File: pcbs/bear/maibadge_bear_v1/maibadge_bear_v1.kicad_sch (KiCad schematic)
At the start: 13 parts, among them J1 Conn_01x04_Socket, SW1 SW_Push, SW2 SW_Push, SW3 SW_Push, SW4 SW_Push, U1 AMS1117-3.3, U2 ESP32-S3-WROOM-1

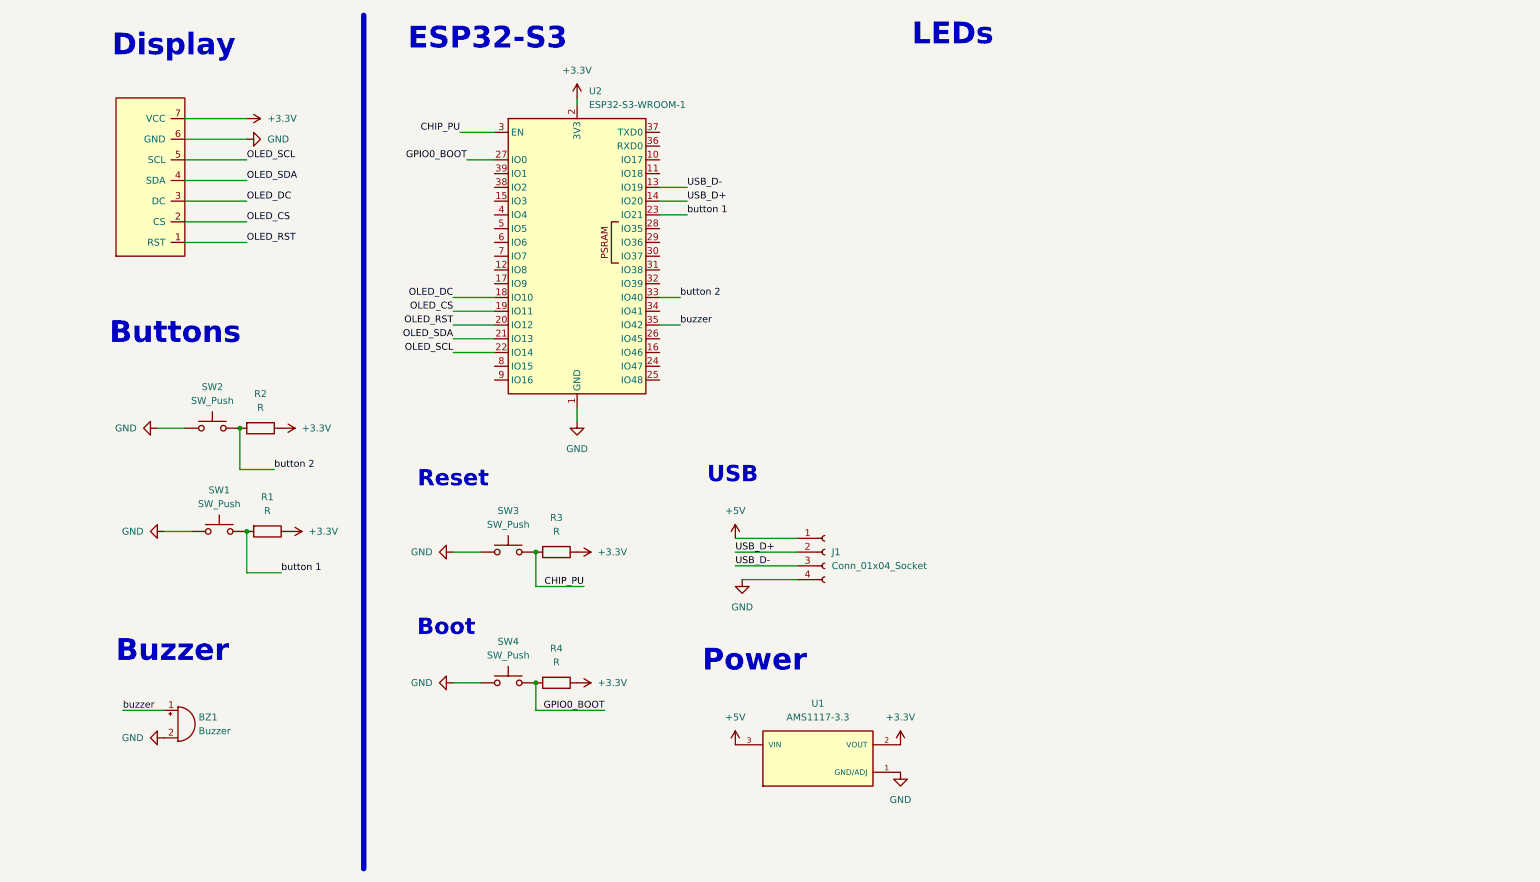
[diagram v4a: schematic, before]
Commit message: added leds and mpr121 for pcb
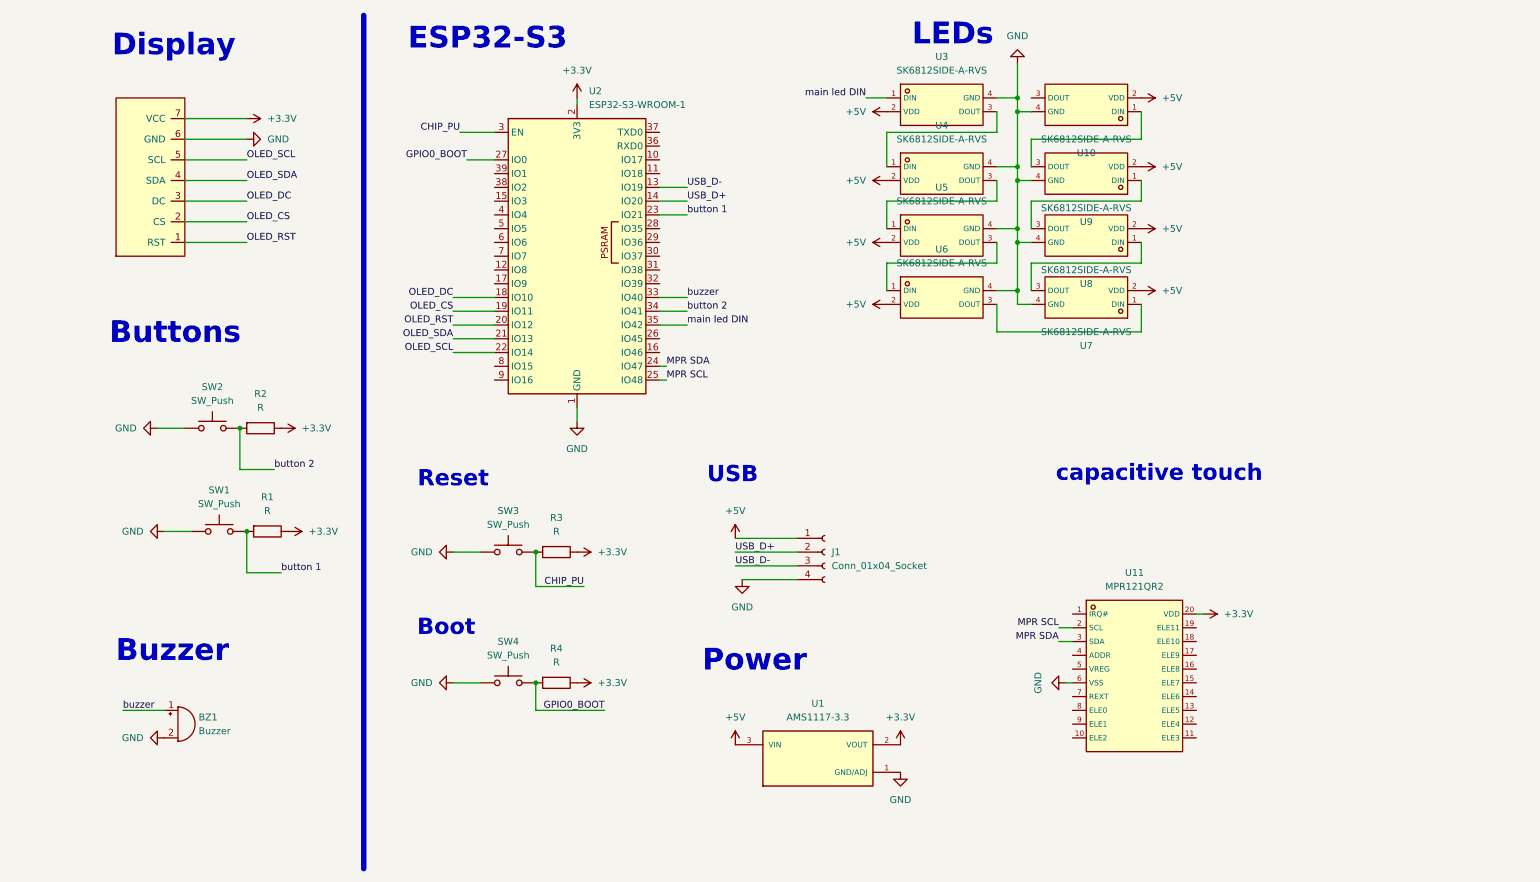
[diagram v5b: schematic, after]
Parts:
- added U10, U3, U4, U5, U6, U7, U8, U9: SK6812SIDE-A-RVS, aeasyeda-footprint:LED-SMD_4P-L4.0-W1.6-L, symbol ask6812:SK6812SIDE-A-RVS
- added U11: MPR121QR2, aeasyeda-footprint:QFN-20_L3.0-W3.0-P0.40-BL, symbol amaibear:MPR121QR2
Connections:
- net +3.3V: now also U11.20 (VDD)
- net +5V: now also U10.2 (VDD), U3.2 (VDD), U4.2 (VDD), U5.2 (VDD), U6.2 (VDD), U7.2 (VDD), U8.2 (VDD), U9.2 (VDD)
- net GND: now also U10.4 (GND), U11.6 (VSS), U3.4 (GND), U4.4 (GND), U5.4 (GND), U6.4 (GND), U7.4 (GND), U8.4 (GND), U9.4 (GND)
- net button 2: now also U2.34 (IO41); no longer U2.33 (IO40)
- net buzzer: now also U2.33 (IO40); no longer U2.35 (IO42)
- net MPR SDA: now reaches U2.24 (IO47)
- net MPR SDA: now also U11.3 (SDA)
- net MPR SCL: now reaches U2.25 (IO48)
- net MPR SCL: now also U11.2 (SCL)
- new net: U3.3 (DOUT), U4.1 (DIN)
- new net: U7.3 (DOUT), U8.1 (DIN)
- new net: U8.3 (DOUT), U9.1 (DIN)
- new net: U5.3 (DOUT), U6.1 (DIN)
- new net: U6.3 (DOUT), U7.1 (DIN)
- new net: U4.3 (DOUT), U5.1 (DIN)
- new net: U10.1 (DIN), U9.3 (DOUT)
- new net main led DIN: U2.35 (IO42), U3.1 (DIN)
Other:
- note added: "capacitive touch"

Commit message: prototype 2 done
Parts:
- removed BZ1: Buzzer, Buzzer_Beeper:MagneticBuzzer_Kobitone_254-EMB73-RO, symbol Device:Buzzer
- removed U11: MPR121QR2, aeasyeda-footprint:QFN-20_L3.0-W3.0-P0.40-BL, symbol amaibear:MPR121QR2
- added JP2: SolderJumper_3_Bridged12, Jumper:SolderJumper-3_P1.3mm_Bridged2Bar12_Pad1.0x1.5mm_NumberLabels, symbol Jumper:SolderJumper_3_Bridged12
- added U12: MS-23C01-G020, aeasyeda-footprint:SW-SMD_G-SWITCH_MS-23C01-G020, symbol amaibear:MS-23C01-G020
- added U13: FUET-7525-3_6V, aeasyeda-footprint:BUZ-SMD_4P-L7.5-W7.5-BR, symbol amaibear:FUET-7525-3_6V
- U1: footprint local_footprints:SOT229P700X180-4N -> aeasyeda-footprint:SOT-89-3_L4.5-W2.5-P1.50-LS4.2-BR
- renumbered U9 to U10, U10 to U3, U3 to U4, U4 to U5, U5 to U6, U6 to U7, U7 to U8, U8 to U9
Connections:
- net MPR SDA is gone; now on net GPIO0_BOOT: U2.24 (IO47)
- net +3.3V: now also JP2.1 (A), U12.2; no longer GC9A01.7 (VCC)
- net +5V: now also JP2.3 (B); no longer U10.2 (VDD), U3.2 (VDD), U4.2 (VDD), U5.2 (VDD), U6.2 (VDD), U7.2 (VDD), U8.2 (VDD), U9.2 (VDD)
- net GND: now also U13.1
- net GPIO0_BOOT: no longer U2.27 (IO0)
- net USB_D+: now also J1.3 (Pin_3), U2.13 (IO19); no longer J1.2 (Pin_2), U2.14 (IO20)
- net USB_D-: now also J1.2 (Pin_2), U2.14 (IO20); no longer J1.3 (Pin_3), U2.13 (IO19)
- net button 2: now also U2.28 (IO35); no longer U2.34 (IO41)
- net buzzer: now also U2.27 (IO0), U13.2; no longer U2.33 (IO40)
- net main led DIN: now also U3.1 (DIN); no longer U4.1 (DIN)
- net touch_sensor_8: now reaches U2.12 (IO8)
- net touch_sensor_3: now reaches U2.15 (IO3)
- net touch_sensor_2: now reaches U2.38 (IO2)
- net touch_sensor_1: now reaches U2.39 (IO1)
- net touch_sensor_4: now reaches U2.4 (IO4)
- net touch_sensor_5: now reaches U2.5 (IO5)
- net touch_sensor_6: now reaches U2.6 (IO6)
- net touch_sensor_7: now reaches U2.7 (IO7)
- net at U10.3 (DOUT): no longer U3.1 (DIN)
- net at U3.3 (DOUT): now also U4.1 (DIN)
- net MPR SCL: no longer names the net of U2.25 (IO48)
- new net: GC9A01.7 (VCC), U12.3
- new net switch-led: JP2.2 (C), U10.2 (VDD), U3.2 (VDD), U4.2 (VDD), U5.2 (VDD), U6.2 (VDD), U7.2 (VDD), U8.2 (VDD), U9.2 (VDD)
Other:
- note removed: "capacitive touch"

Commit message: prototype 2 rehaul finished
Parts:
- removed R2: R, Resistor_SMD:R_0805_2012Metric_Pad1.20x1.40mm_HandSolder, symbol Device:R
- removed SW2: SW_Push, Button_Switch_SMD:SW_Push_1P1T_XKB_TS-1187A, symbol Switch:SW_Push
- renumbered U3 to U10, U10 to U3, U9 to U4, U8 to U5, U7 to U6, U6 to U7, U5 to U8, U4 to U9
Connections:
- net GPIO0_BOOT: now also U2.27 (IO0); no longer U2.24 (IO47)
- net USB_D+: now also U2.14 (IO20); no longer U2.13 (IO19)
- net USB_D-: now also U2.13 (IO19); no longer U2.14 (IO20)
- net button 1: now also U2.17 (IO9); no longer U2.23 (IO21)
- net buzzer: now also U2.24 (IO47); no longer U2.27 (IO0)
- net main led DIN: now also U2.8 (IO15), U3.1 (DIN); no longer U10.1 (DIN), U2.35 (IO42)
- net at U9.1 (DIN): now also U8.3 (DOUT); no longer U10.3 (DOUT)
- net at U9.3 (DOUT): now also U10.1 (DIN); no longer U8.1 (DIN)
- net at U4.1 (DIN): now also U3.3 (DOUT); no longer U5.3 (DOUT)
- net at U4.3 (DOUT): now also U5.1 (DIN); no longer U3.1 (DIN)
- net at U6.1 (DIN): now also U5.3 (DOUT); no longer U7.3 (DOUT)
- net at U6.3 (DOUT): now also U7.1 (DIN); no longer U5.1 (DIN)
- net button 2: no longer names the net of U2.28 (IO35)
- new net: U7.3 (DOUT), U8.1 (DIN)
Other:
- note added: "Debugging Buttons"
- note added: "Swap between 3.3V and 5V for LEDs"
- note removed: "Buttons"
- moved on the sheet: R1, SW1, U13, U3, U4, U5, U6, U7, U8, U9

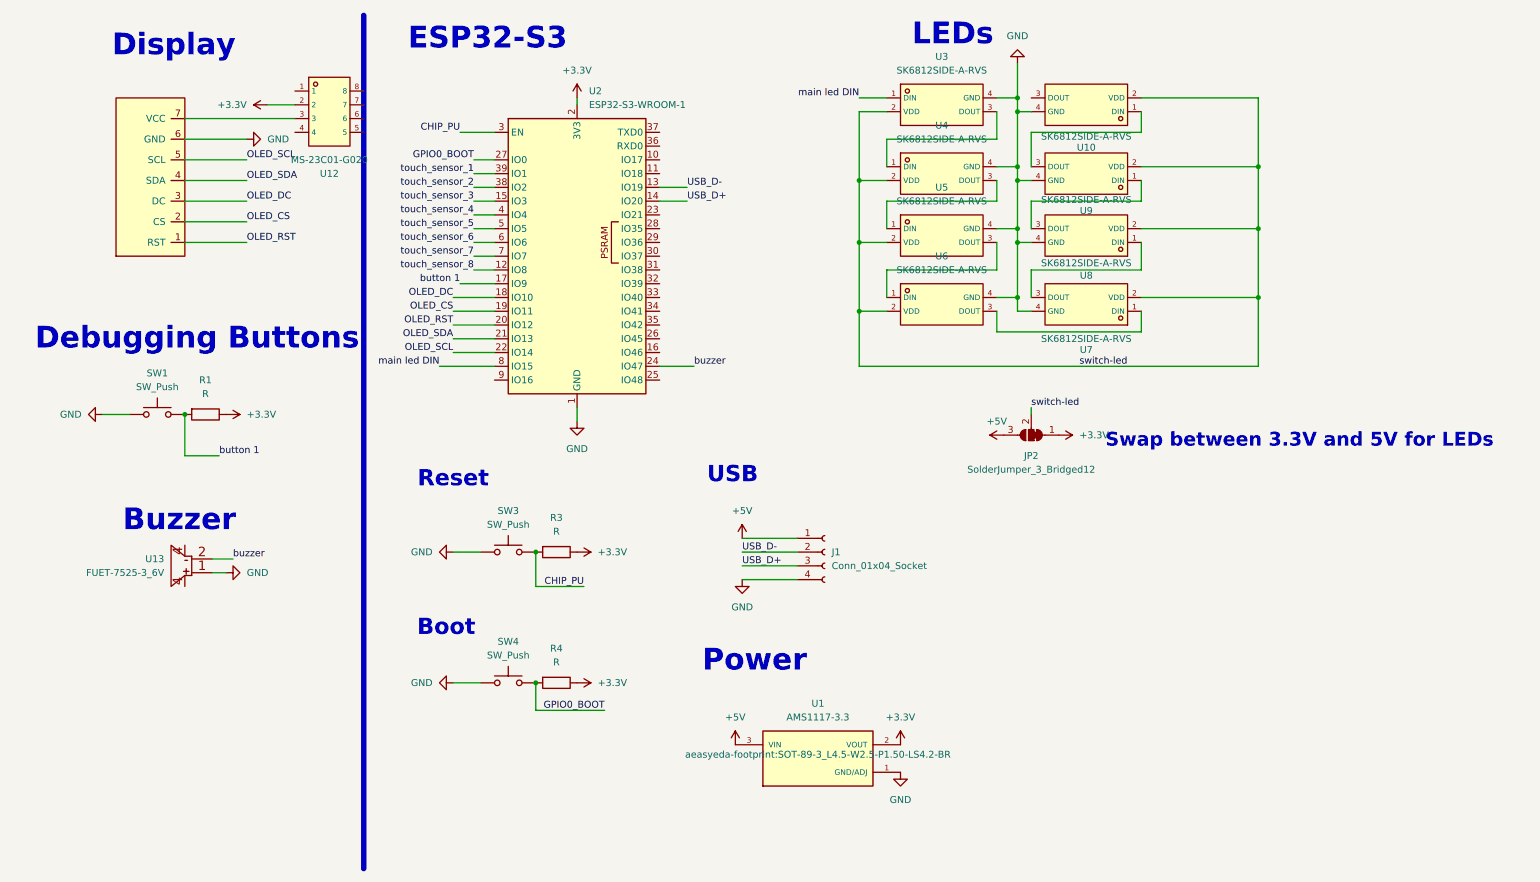
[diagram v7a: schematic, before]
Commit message: feat: power fixes and touchpad routing
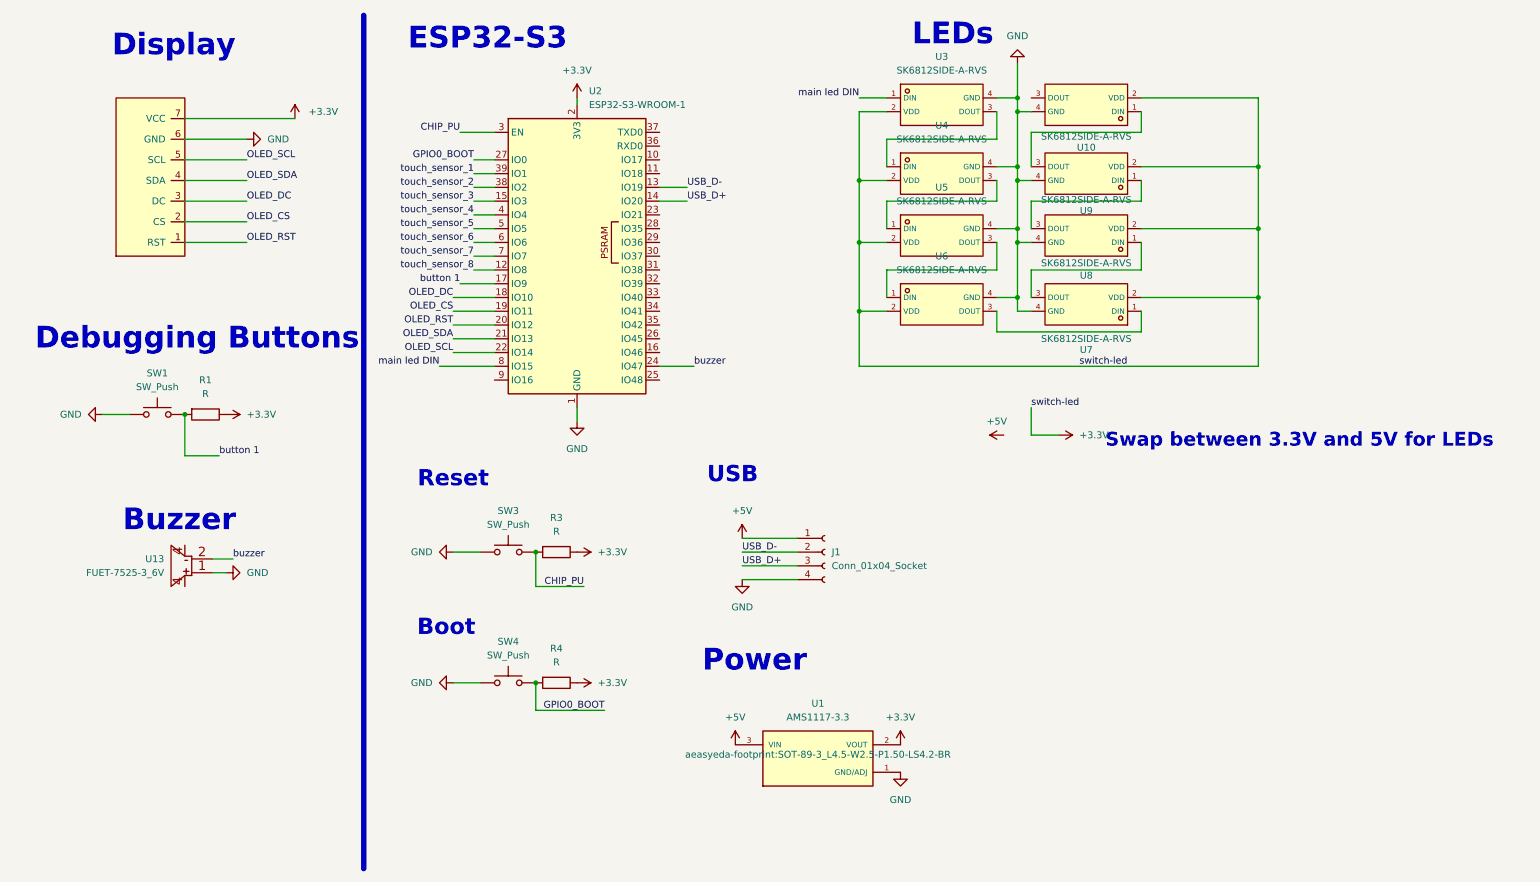
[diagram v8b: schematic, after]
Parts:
- removed JP2: SolderJumper_3_Bridged12, Jumper:SolderJumper-3_P1.3mm_Bridged2Bar12_Pad1.0x1.5mm_NumberLabels, symbol Jumper:SolderJumper_3_Bridged12
- removed U12: MS-23C01-G020, aeasyeda-footprint:SW-SMD_G-SWITCH_MS-23C01-G020, symbol amaibear:MS-23C01-G020
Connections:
- net switch-led is gone; now on net +3.3V: U10.2 (VDD), U3.2 (VDD), U4.2 (VDD), U5.2 (VDD), U6.2 (VDD), U7.2 (VDD), U8.2 (VDD), U9.2 (VDD)
- net +3.3V: now also GC9A01.7 (VCC)
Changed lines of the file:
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@@
-	(wire
-		(pts
-			(xy 52.07 33.02) (xy 57.15 33.02)
-		)
-		(stroke
-			(width 0)
-			(type default)
-		)
-	)
 	(wire
 		(pts
@@
 	(wire
 		(pts
+			(xy 193.04 88.9) (xy 193.04 93.98)
+		)
+		(stroke
+			(width 0)
+			(type default)
+		)
+	)
+	(wire
+		(pts
 			(xy 190.5 34.29) (xy 190.5 44.45)
 		)
@@
 	(wire
 		(pts
+			(xy 193.04 93.98) (xy 198.12 93.98)
+		)
+		(stroke
+			(width 0)
+			(type default)
+		)
+	)
+	(wire
+		(pts
 			(xy 186.69 55.88) (xy 190.5 55.88)
 		)
@@
 		(pts
 			(xy 36.83 58.42) (xy 48.26 58.42)
-		)
-		(stroke
-			(width 0)
-			(type default)
-		)
-	)
-	(wire
-		(pts
-			(xy 193.04 88.9) (xy 193.04 90.17)
 		)
 		(stroke
@@
 			)
 			(justify left bottom)
-		)
-	)
-	(symbol
-		(lib_id "Jumper:SolderJumper_3_Bridged12")
-		(at 193.04 93.98 180)
-		(unit 1)
-		(exclude_from_sim yes)
-		(in_bom no)
-		(on_board yes)
-		(dnp no)
-		(fields_autoplaced yes)
-		(property "Reference" "JP2"
-			(at 193.04 97.79 0)
-			(effects
-				(font
-					(size 1.27 1.27)
-				)
-			)
-		)
-		(property "Value" "SolderJumper_3_Bridged12"
-			(at 193.04 100.33 0)
-			(effects
-				(font
-					(size 1.27 1.27)
-				)
-			)
-		)
-		(property "Footprint" "Jumper:SolderJumper-3_P1.3mm_Bridged2Bar12_Pad1.0x1.5mm_NumberLabels"
-			(at 193.04 93.98 0)
-			(effects
-				(font
-					(size 1.27 1.27)
-				)
-				(hide yes)
-			)
-		)
-		(property "Datasheet" "~"
-			(at 193.04 93.98 0)
-			(effects
-				(font
-					(size 1.27 1.27)
-				)
-				(hide yes)
-			)
-		)
-		(property "Description" "3-pole Solder Jumper, pins 1+2 closed/bridged"
-			(at 193.04 93.98 0)
-			(effects
-				(font
-					(size 1.27 1.27)
-				)
-				(hide yes)
-			)
-		)
-		(pin "1"
-		)
-		(pin "3"
-		)
-		(pin "2"
-		)
-		(instances
-			(project ""
-				(path "/8829ea97-d982-42a1-8001-8683a28d2262"
-					(reference "JP2")
-					(unit 1)
-				)
-			)
-		)
-	)
-	(symbol
-		(lib_id "amaibear:MS-23C01-G020")
-		(at 62.23 35.56 90)
-		(mirror x)
-		(unit 1)
-		(exclude_from_sim no)
-		(in_bom yes)
-		(on_board yes)
-		(dnp no)
-		(property "Reference" "U12"
-			(at 63.5 45.72 90)
-			(effects
-				(font
-					(size 1.27 1.27)
-				)
-			)
-		)
-		(property "Value" "MS-23C01-G020"
-			(at 63.5 43.18 90)
-			(effects
-				(font
-					(size 1.27 1.27)
-				)
-			)
-		)
-		(property "Footprint" "aeasyeda-footprint:SW-SMD_G-SWITCH_MS-23C01-G020"
-			(at 72.39 35.56 0)
-			(effects
-				(font
-					(size 1.27 1.27)
-					(italic yes)
-				)
-				(hide yes)
-			)
-		)
-		(property "Datasheet" "https://dg-conn.com/uploads/soft/170113/MS-23C01-GXXX.pdf"
-			(at 62.103 33.274 0)
-			(effects
-				(font
-					(size 1.27 1.27)
-				)
-				(justify left)
-				(hide yes)
-			)
-		)
-		(property "Description" ""
-			(at 62.23 35.56 0)
-			(effects
-				(font
-					(size 1.27 1.27)
-				)
-				(hide yes)
-			)
-		)
-		(property "LCSC" "C2896620"
-			(at 62.23 35.56 0)
-			(effects
-				(font
-					(size 1.27 1.27)
-				)
-				(hide yes)
-			)
-		)
-		(pin "6"
-		)
-		(pin "1"
-		)
-		(pin "2"
-		)
-		(pin "4"
-		)
-		(pin "7"
-		)
-		(pin "8"
-		)
-		(pin "5"
-		)
-		(pin "3"
-		)
-		(instances
-			(project "maibadge_bear_v1"
-				(path "/8829ea97-d982-42a1-8001-8683a28d2262"
-					(reference "U12")
-					(unit 1)
-				)
-			)
 		)
 	)
@@
 	(symbol
 		(lib_id "power:+3.3V")
-		(at 52.07 33.02 90)
+		(at 57.15 35.56 0)
 		(unit 1)
 		(exclude_from_sim no)
@@
 		(fields_autoplaced yes)
 		(property "Reference" "#PWR01"
-			(at 55.88 33.02 0)
+			(at 57.15 39.37 0)
 			(effects
 				(font
@@
 		)
 		(property "Value" "+3.3V"
-			(at 48.26 33.0199 90)
+			(at 59.69 34.2899 0)
 			(effects
 				(font
@@
 		)
 		(property "Footprint" ""
-			(at 52.07 33.02 0)
+			(at 57.15 35.56 0)
 			(effects
 				(font
@@
 		)
 		(property "Datasheet" ""
-			(at 52.07 33.02 0)
+			(at 57.15 35.56 0)
 			(effects
 				(font
@@
 		)
 		(property "Description" "Power symbol creates a global label with name \"+3.3V\""
-			(at 52.07 33.02 0)
-			(effects
-				(font
+			(at 57.15 35.56 0)
+			(effects
+				(font
